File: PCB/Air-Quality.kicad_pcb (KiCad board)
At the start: 2 copper layers, 62 x 25.7 mm, 18 parts, among them J2 Conn_01x04_Female, J3 Conn_01x07_Female, SW1 SW_Push, SW2 SW_SPST, U1 ARDUINO_MKR_ZERO

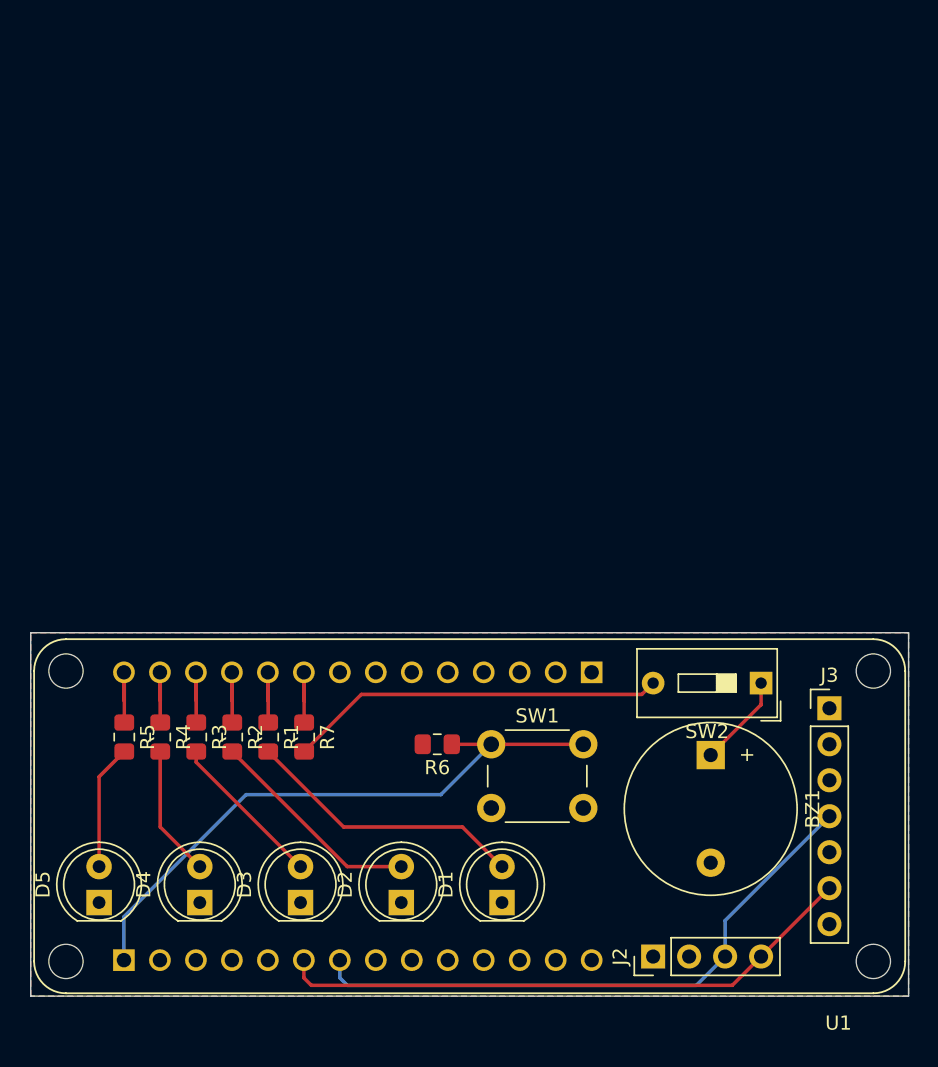
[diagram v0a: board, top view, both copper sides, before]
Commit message: changed to RP 2040.
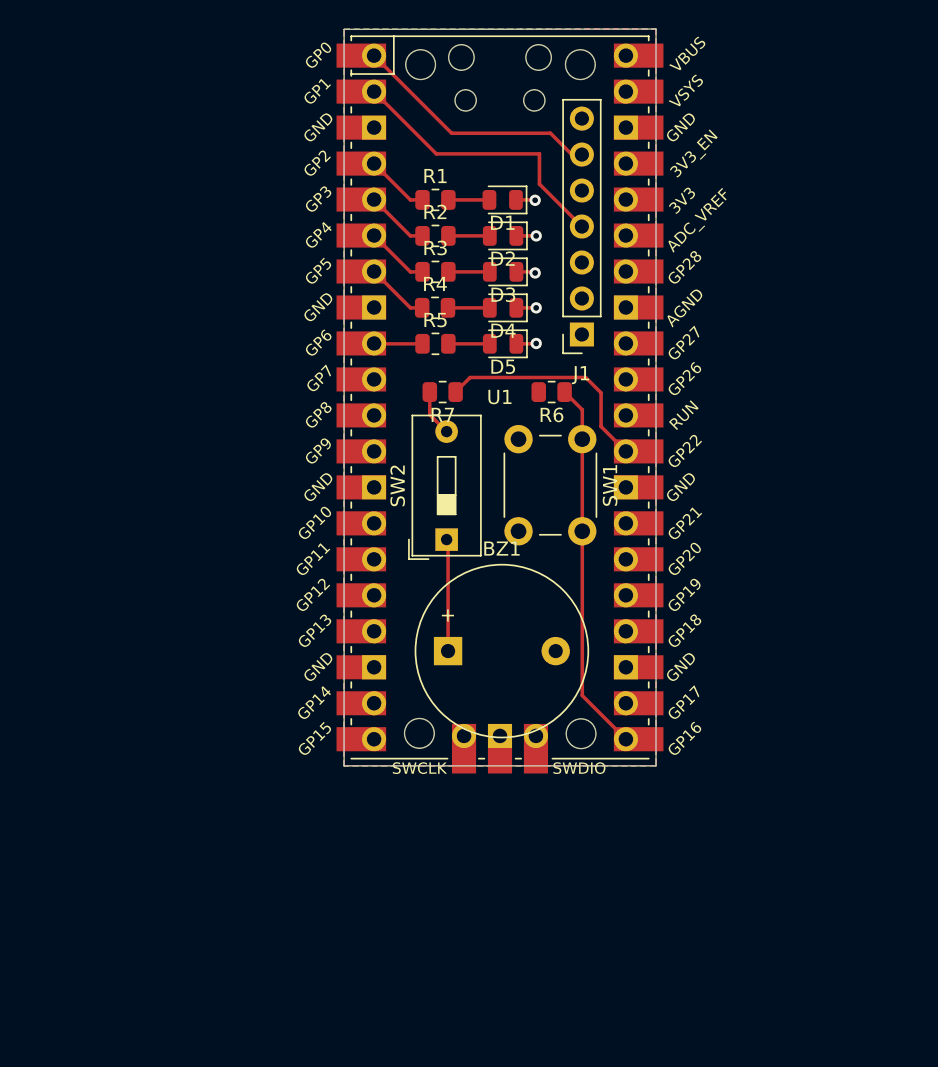
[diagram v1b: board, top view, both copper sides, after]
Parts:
- removed J2: Conn_01x04_Female, Connector_PinHeader_2.54mm:PinHeader_1x04_P2.54mm_Vertical
- removed J3: Conn_01x07_Female, Connector_PinHeader_2.54mm:PinHeader_1x07_P2.54mm_Vertical
- added J1: Conn_01x07_Female, Connector_PinSocket_2.54mm:PinSocket_1x07_P2.54mm_Vertical, F.Cu at (192.6, 83.8)
- D1, D2, D3, D4, D5: footprint LED_THT:LED_D5.0mm_Clear -> LED_SMD:LED_0805_2012Metric
- R1, R2, R3, R4, R5, R6, R7: footprint Resistor_SMD:R_0805_2012Metric_Pad1.15x1.40mm_HandSolder -> Resistor_SMD:R_0805_2012Metric
- U1: value ARDUINO_MKR_ZERO -> Pico; footprint Arduino-MKR:MODULE_ARDUINO_MKR_ZERO -> MCU_RaspberryPI_and_Board:RPi_Pico_SMD_TH
- moved D1 49.6 mm to (187.0, 74.3), turned to 180 degrees
- moved D5 48.7 mm to (187.0, 84.5), turned to 180 degrees
- moved D2 47.6 mm to (187.0, 76.9), turned to 180 degrees
- moved D4 47.1 mm to (187.0, 82.0), turned to 180 degrees
- moved D3 46.8 mm to (187.0, 79.4), turned to 180 degrees
- moved R1 39.7 mm to (182.2, 74.3), turned to 0 degrees
- moved R2 38.2 mm to (182.2, 76.9), turned to 0 degrees
- moved R3 36.9 mm to (182.2, 79.4), turned to 0 degrees
- moved R4 36.0 mm to (182.2, 82.0), turned to 0 degrees
- moved R5 35.4 mm to (182.2, 84.5), turned to 0 degrees
- moved U1 29.6 mm to (186.8, 88.3), turned to 0 degrees
- moved R7 26.2 mm to (182.8, 87.9), turned to 180 degrees
- moved R6 26.1 mm to (190.4, 87.9)
- moved SW2 24.4 mm to (183.0, 98.3), turned to 90 degrees
- moved SW1 22.5 mm to (192.6, 91.2), turned to 270 degrees
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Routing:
- net /SDA: track 41.4 -> 17.6 mm
- net Net-(R7-Pad2): track 26.6 -> 3.32 mm
- net /SCL: track 42.5 -> 19.9 mm
- net Net-(R6-Pad1): track 43.3 -> 26.3 mm
- net Net-(D1-Pad2): track 19.9 -> 2.90 mm
- net Net-(D2-Pad2): track 15.3 -> 2.92 mm
- net Net-(R7-Pad1): track 5.69 -> 16.0 mm
- net Net-(D3-Pad2): track 11.2 -> 2.93 mm
- net GND: track 0.00 -> 6.93 mm, vias 0 -> 5
- net Net-(D4-Pad2): track 9.28 -> 2.95 mm
- net Net-(D5-Pad2): track 8.86 -> 2.93 mm
- net Net-(R5-Pad1): track 5.69 -> 3.43 mm
- net Net-(R4-Pad1): track 5.69 -> 4.46 mm
- net Net-(R3-Pad1): track 5.69 -> 4.48 mm
- net Net-(R2-Pad1): track 5.69 -> 4.48 mm
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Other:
- board size 62 x 25.7 mm -> 22 x 52 mm

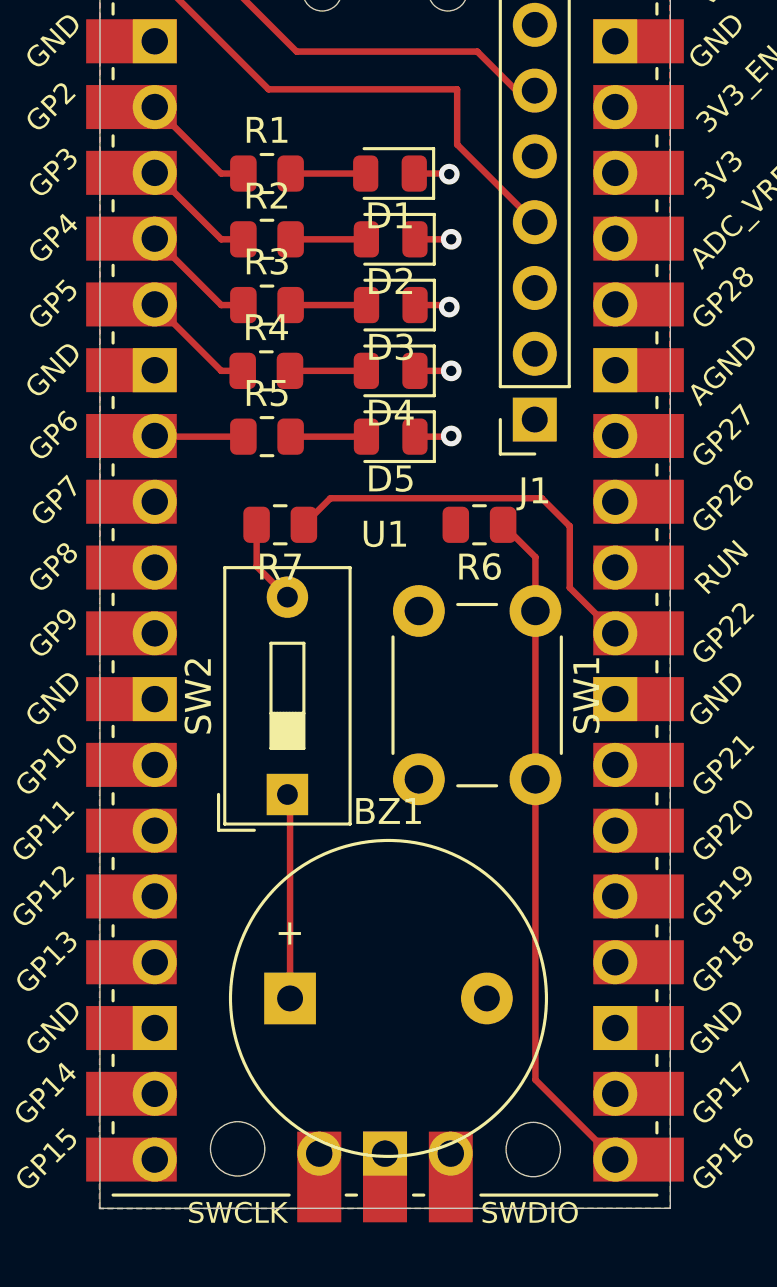
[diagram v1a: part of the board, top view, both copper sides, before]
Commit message: Small Buzzer. Wrong Sensor Configuration :-(
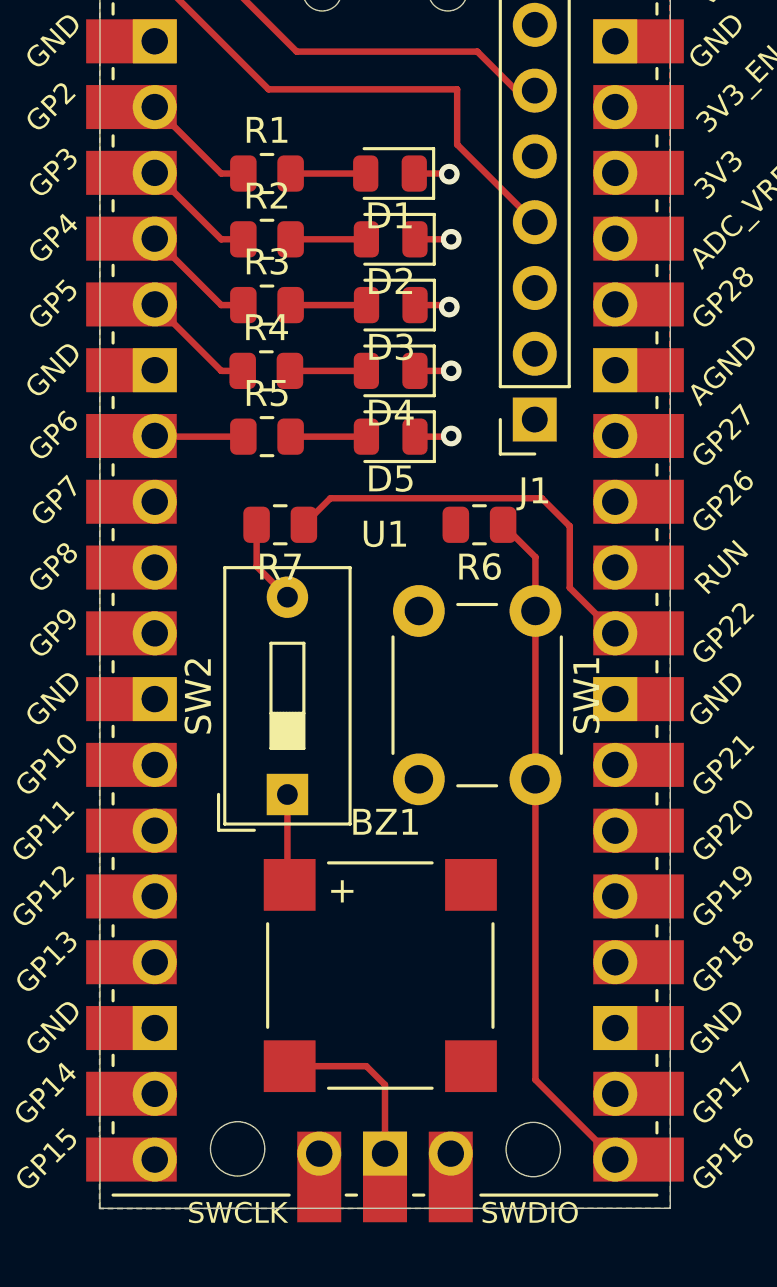
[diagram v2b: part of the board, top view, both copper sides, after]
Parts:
- BZ1: footprint Buzzer_Beeper:Buzzer_12x9.5RM7.6 -> Buzzer_Beeper:PUIAudio_SMT_0825_S_4_R
- moved BZ1 3.60 mm to (186.6, 105.3)
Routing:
- net GND: track 6.93 -> 13.6 mm
- net Net-(BZ1-Pad1): track 7.60 -> 3.63 mm
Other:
- rule pad_to_mask_clearance: 0.05 -> 0

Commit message: Version 3 for friends.
Seeeduino
New Sensor
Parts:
- removed D1, D2, D3, D4, D5: LED, LED_SMD:LED_0805_2012Metric
- removed R1, R2, R3, R4, R5: 220 Ohm, Resistor_SMD:R_0805_2012Metric
- removed R6: 10kOhm, Resistor_SMD:R_0805_2012Metric
- removed SW1: SW_Push, Button_Switch_THT:SW_PUSH_6mm
- added H1: MountingHole, MountingHole:MountingHole_2.7mm_M2.5_ISO14580, F.Cu at (116.8, 33.1)
- added H2: MountingHole, MountingHole:MountingHole_2.7mm_M2.5_ISO14580, F.Cu at (116.5, 60.2)
- added H3: MountingHole, MountingHole:MountingHole_2.7mm_M2.5_ISO14580, F.Cu at (157.7, 33.1)
- added H4: MountingHole, MountingHole:MountingHole_2.7mm_M2.5_ISO14580, F.Cu at (157.7, 60.1)
- U1: value Pico -> SeeeduinoXIAO; footprint MCU_RaspberryPI_and_Board:RPi_Pico_SMD_TH -> Seeeduino XIAO KICAD:Seeeduino XIAO-MOUDLE14P-2.54-21X17.8MM
- moved J1 71.4 mm to (137.3, 38.6), turned to 90 degrees
- moved BZ1 66.4 mm to (145.1, 53.5), turned to 270 degrees
- moved U1 62.5 mm to (133.6, 55.5), turned to 90 degrees
- moved R7 55.0 mm to (151.9, 42.4), turned to 0 degrees
- moved SW2 54.4 mm to (158.2, 49.9)
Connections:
- J1 pad 1: +3V3 -> GND
- J1 pad 3: GND -> +3V3
- J1 pad 5: Net-(J1-Pad5) -> /SDA
- J1 pad 6: /SDA -> Net-(J1-Pad6)
- U1 pad 1: /SDA -> Net-(R7-Pad1)
- U1 pad 12: Net-(U1-Pad12) -> +3V3
- U1 pad 16: Net-(U1-Pad16) -> GND
- U1 pad 18: GND -> Net-(U1-Pad18)
- U1 pad 2: /SCL -> Net-(U1-Pad2)
- U1 pad 20: Net-(U1-Pad20) -> GND
- U1 pad 3: GND -> Net-(U1-Pad3)
- U1 pad 5: Net-(R2-Pad1) -> /SDA
- U1 pad 6: Net-(R3-Pad1) -> /SCL
- U1 pad 8: GND -> Net-(U1-Pad8)
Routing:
- net Net-(R7-Pad1): track 16.0 -> 45.3 mm
- net Net-(R6-Pad1): track 26.3 -> 0.00 mm
- net +3V3: track 0.00 -> 24.9 mm
- net /SDA: track 17.6 -> 31.6 mm
- net GND: track 13.6 -> 22.3 mm, vias 5 -> 0
- net Net-(BZ1-Pad1): track 3.63 -> 9.58 mm
- net Net-(U1-Pad4): track 4.48 -> 0.00 mm
- net Net-(R3-Pad1): track 4.48 -> 0.00 mm
- net Net-(R2-Pad1): track 4.48 -> 0.00 mm
- net Net-(U1-Pad7): track 4.46 -> 0.00 mm
- net /SCL: track 19.9 -> 23.4 mm
- net Net-(U1-Pad9): track 3.43 -> 0.00 mm
- net Net-(D4-Pad2): track 2.95 -> 0.00 mm
- net Net-(D3-Pad2): track 2.93 -> 0.00 mm
- net Net-(D5-Pad2): track 2.93 -> 0.00 mm
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- added copper zone on F.Cu, net GND
- removed copper zone on F.Cu, net +3V3
- removed copper zone on B.Cu, net GND
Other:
- board size 22 x 52 mm -> 48.5 x 33.1 mm
